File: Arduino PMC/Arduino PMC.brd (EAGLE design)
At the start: 15.6 x 33.7 mm, 28 parts, among them U2 MIC5219, U3 ATMEGA32U4, X1 USB-MICROB, Y1 16MHz

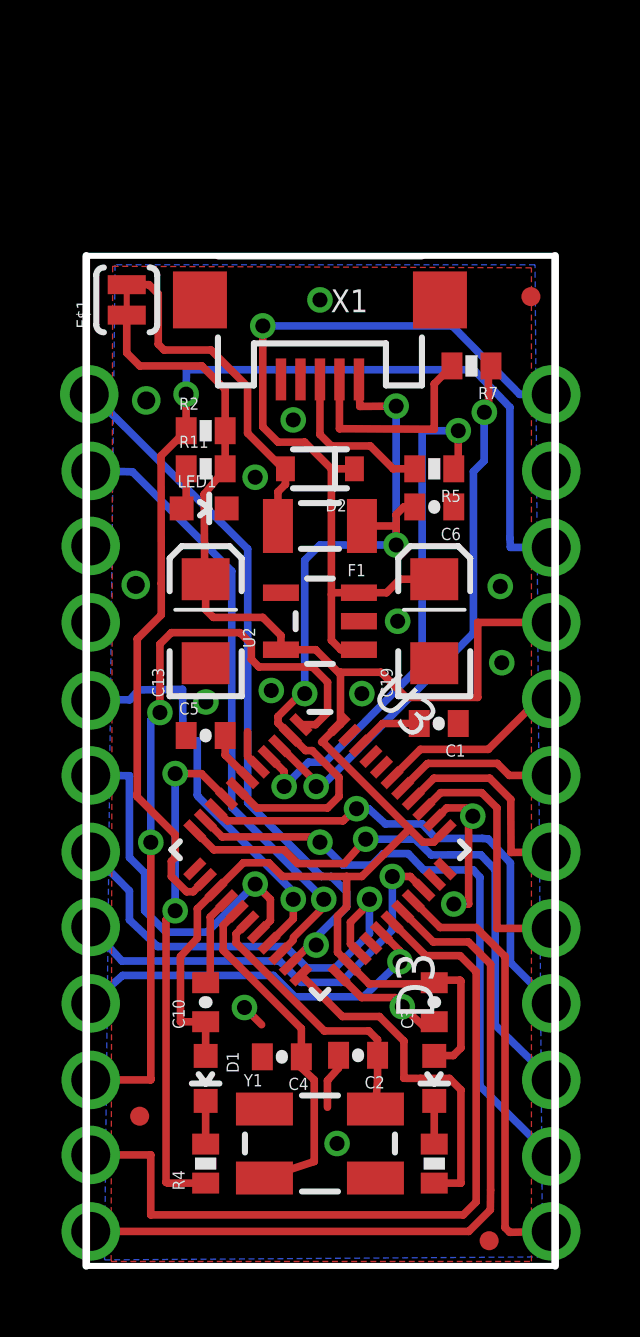
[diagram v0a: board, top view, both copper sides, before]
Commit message: Added USB PCB connector to Arduino PMC
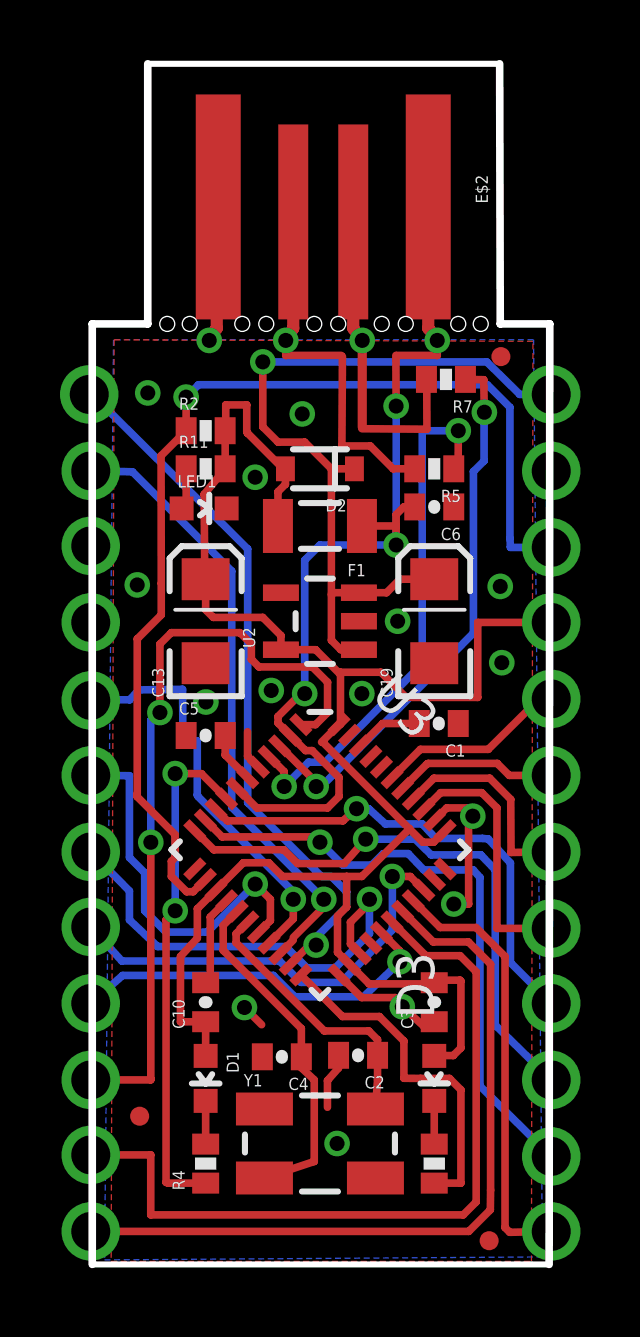
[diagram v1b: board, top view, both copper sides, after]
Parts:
- removed E$1: (no value), SparkFun:SJ_2S-TRACE
- removed X1: USB-MICROB, SparkFun:USB-MICROB
- added E$2: (no value), SparkFun-Connectors:USB-A-PCB
- moved JP2 2.24 mm to (15.5, 30.9)
- moved R7 0.96 mm to (13.6, 30.1)
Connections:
- removed net N$3: D2.2, E$1.2, F1.2
- new net S$4: D2.2, F1.2
- net GND: no longer X1.GND
- net N$6: no longer X1.D-
- net N$8: no longer X1.D+
- net UVCC: no longer X1.VBUS
- net VCC: no longer E$1.1
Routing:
- net N$3: track 11.7 -> 0.00 mm
- net VCC: track 62.0 -> 55.7 mm
- net S$2: track 0.00 -> 3.90 mm, vias 0 -> 1
- net S$4: track 0.00 -> 3.78 mm
- net N$6: track 7.16 -> 3.83 mm
- net S$7: track 0.00 -> 2.25 mm
- net S$5: track 0.00 -> 2.00 mm
- net S$6: track 0.00 -> 1.80 mm
- net RAW: track 28.0 -> 26.3 mm
- net GND: track 16.0 -> 17.2 mm
- net S$3: track 0.00 -> 1.07 mm, vias 0 -> 1
- net S$1: track 0.00 -> 1.01 mm
- net RESET: track 37.0 -> 36.1 mm
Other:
- board size 15.6 x 33.7 mm -> 15.3 x 40 mm

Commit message: Adjust board length, traces, breakaway connector, and added pogo pin vias
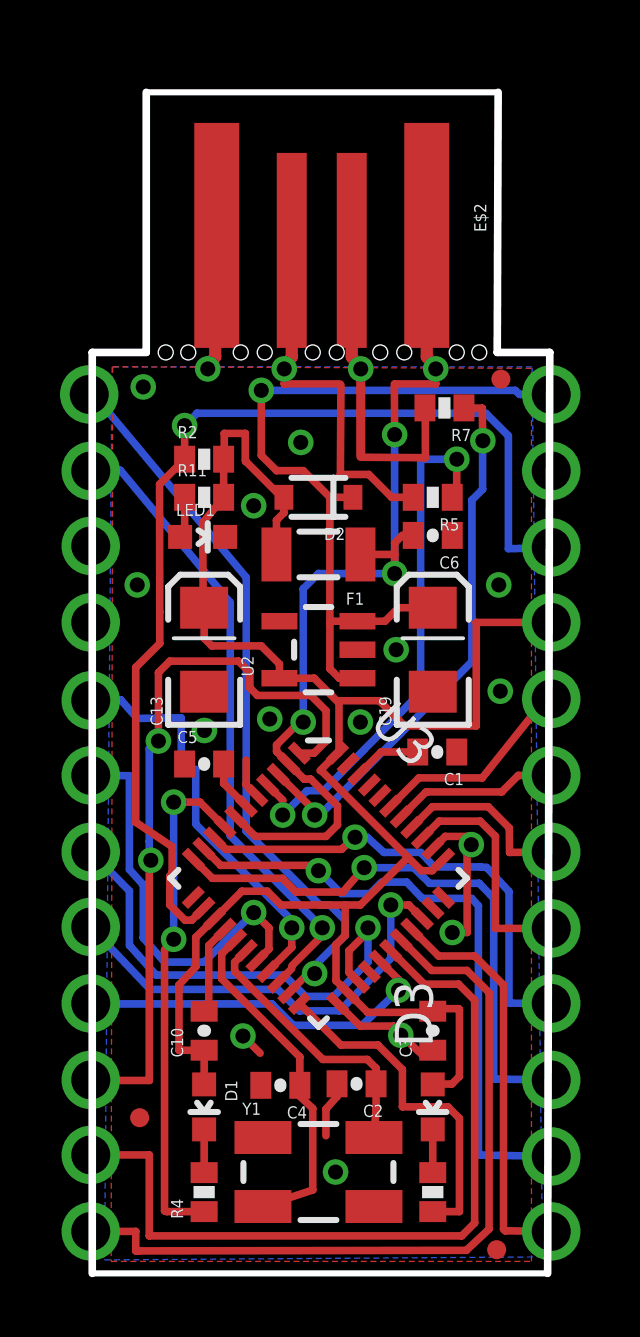
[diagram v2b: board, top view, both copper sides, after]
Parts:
- moved C6 0.95 mm to (13.2, 24.9)
- moved R7 0.95 mm to (13.6, 29.1)
- moved C2 0.95 mm to (10.7, 6.62)
- moved D1 0.95 mm to (5.58, 5.85)
- moved D3 0.95 mm to (13.2, 5.85)
- moved R4 0.95 mm to (5.58, 3.01)
- moved R6 0.95 mm to (13.2, 3.01)
- moved Y1 0.95 mm to (9.39, 3.68)
- moved C1 0.95 mm to (13.3, 17.7)
- moved C10 0.95 mm to (5.58, 8.39)
- moved C13 0.95 mm to (5.58, 21.1)
- moved C19 0.95 mm to (13.2, 21.1)
- moved C3 0.95 mm to (13.2, 8.39)
- moved C4 0.95 mm to (8.12, 6.57)
- moved C5 0.95 mm to (5.58, 17.3)
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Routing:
- net VCC: track 55.7 -> 56.7 mm
- net D3: track 12.6 -> 13.6 mm
- net A0: track 8.71 -> 7.81 mm
- net A1: track 6.94 -> 6.04 mm
- net D10: track 14.5 -> 13.6 mm
- net D4: track 15.3 -> 16.2 mm
- net D7: track 25.5 -> 24.6 mm
- net RESET: track 36.1 -> 35.3 mm
- net TXO: track 23.7 -> 24.4 mm
- net A3: track 6.37 -> 7.01 mm
- net RXI: track 20.7 -> 21.3 mm
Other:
- board size 15.3 x 40 mm -> 15.3 x 39.4 mm
